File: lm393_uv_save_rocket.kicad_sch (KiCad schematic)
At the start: 13 parts, among them J1 BAT 9V, J2 IGNITER, Q1 TIP122, U1 LM7805, U2 LM393

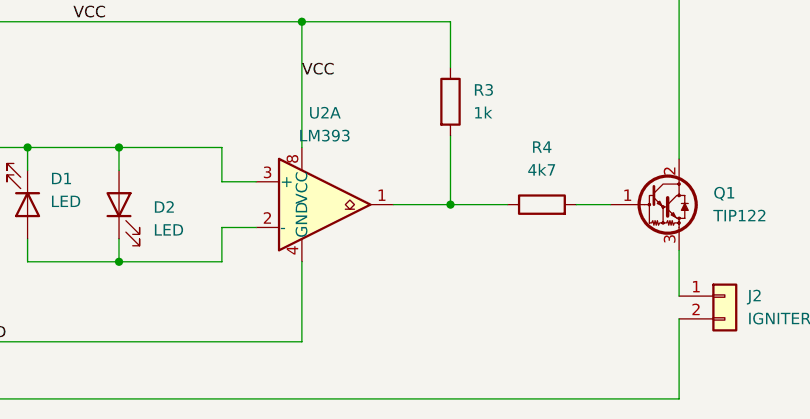
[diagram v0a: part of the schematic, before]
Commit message: Novo led que informa posição correta dos led UV, e funcionamento do circuito
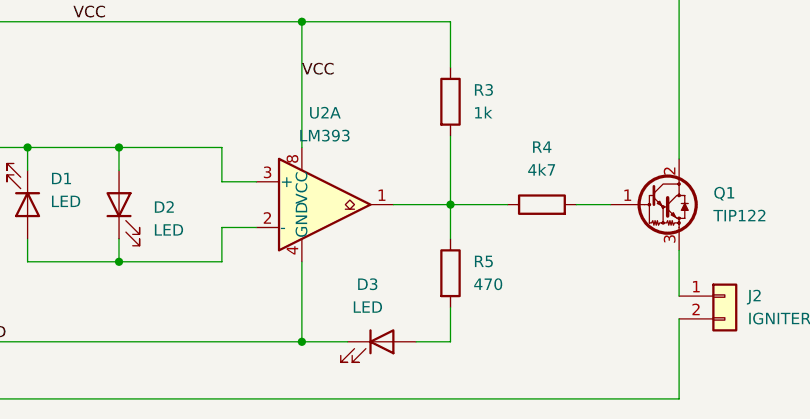
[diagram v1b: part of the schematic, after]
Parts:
- added D3: LED, LED_THT:LED_D5.0mm, symbol Device:LED
- added R5: 470, Resistor_THT:R_Axial_DIN0204_L3.6mm_D1.6mm_P5.08mm_Horizontal, symbol Device:R
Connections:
- net GND: now also D3.1 (K)
- net at R3.2, R4.1, U2.1: now also R5.1
- new net: D3.2 (A), R5.2
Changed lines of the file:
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@@
+	)
+	(junction
+		(at 129.54 63.5)
+		(diameter 0)
+		(color 0 0 0 0)
 	)
 	(junction
@@
 	(wire
 		(pts
+			(xy 146.05 48.26) (xy 146.05 52.07)
+		)
+		(stroke
+			(width 0)
+			(type default)
+		)
+	)
+	(wire
+		(pts
+			(xy 142.24 63.5) (xy 146.05 63.5)
+		)
+		(stroke
+			(width 0)
+			(type default)
+		)
+	)
+	(wire
+		(pts
 			(xy 29.21 21.59) (xy 171.45 21.59)
 		)
@@
 		(pts
 			(xy 52.07 38.1) (xy 44.45 38.1)
+		)
+		(stroke
+			(width 0)
+			(type default)
+		)
+	)
+	(wire
+		(pts
+			(xy 146.05 63.5) (xy 146.05 59.69)
+		)
+		(stroke
+			(width 0)
+			(type default)
+		)
+	)
+	(wire
+		(pts
+			(xy 129.54 63.5) (xy 134.62 63.5)
 		)
 		(stroke
@@
 	)
 	(symbol
+		(lib_id "Device:R")
+		(at 146.05 55.88 0)
+		(unit 1)
+		(exclude_from_sim no)
+		(in_bom yes)
+		(on_board yes)
+		(dnp no)
+		(fields_autoplaced yes)
+		(property "Reference" "R5"
+			(at 148.59 54.6099 0)
+			(effects
+				(font
+					(size 1.27 1.27)
+				)
+				(justify left)
+			)
+		)
+		(property "Value" "470"
+			(at 148.59 57.1499 0)
+			(effects
+				(font
+					(size 1.27 1.27)
+				)
+				(justify left)
+			)
+		)
+		(property "Footprint" "Resistor_THT:R_Axial_DIN0204_L3.6mm_D1.6mm_P5.08mm_Horizontal"
+			(at 144.272 55.88 90)
+			(effects
+				(font
+					(size 1.27 1.27)
+				)
+				(hide yes)
+			)
+		)
+		(property "Datasheet" "~"
+			(at 146.05 55.88 0)
+			(effects
+				(font
+					(size 1.27 1.27)
+				)
+				(hide yes)
+			)
+		)
+		(property "Description" "Resistor"
+			(at 146.05 55.88 0)
+			(effects
+				(font
+					(size 1.27 1.27)
+				)
+				(hide yes)
+			)
+		)
+		(pin "1"
+		)
+		(pin "2"
+		)
+		(instances
+			(project ""
+				(path "/ae093865-4f5b-4e6d-9eba-48d65543423e"
+					(reference "R5")
+					(unit 1)
+				)
+			)
+		)
+	)
+	(symbol
 		(lib_id "Comparator:LM393")
 		(at 132.08 48.26 0)
@@
 					(unit 1)
 				)
+			)
+		)
+	)
+	(symbol
+		(lib_id "Device:LED")
+		(at 138.43 63.5 0)
+		(unit 1)
+		(exclude_from_sim no)
+		(in_bom yes)
+		(on_board yes)
+		(dnp no)
+		(fields_autoplaced yes)
+		(property "Reference" "D3"
+			(at 136.8425 57.15 0)
+			(effects
+				(font
+					(size 1.27 1.27)
+				)
+			)
+		)
+		(property "Value" "LED"
+			(at 136.8425 59.69 0)
+			(effects
+				(font
+					(size 1.27 1.27)
+				)
+			)
+		)
+		(property "Footprint" "LED_THT:LED_D5.0mm"
+			(at 138.43 63.5 0)
+			(effects
+				(font
+					(size 1.27 1.27)
+				)
+				(hide yes)
+			)
+		)
+		(property "Datasheet" "~"
+			(at 138.43 63.5 0)
+			(effects
+				(font
+					(size 1.27 1.27)
+				)
+				(hide yes)
+			)
+		)
+		(property "Description" "Light emitting diode"
+			(at 138.43 63.5 0)
+			(effects
+				(font
+					(size 1.27 1.27)
+				)
+				(hide yes)
+			)
+		)
+		(property "Sim.Pins" "1=K 2=A"
+			(at 138.43 63.5 0)
+			(effects
+				(font
+					(size 1.27 1.27)
+				)
+				(hide yes)
+			)
+		)
+		(pin "1"
+		)
+		(pin "2"
+		)
+		(instances
+			(project ""
+				(path "/ae093865-4f5b-4e6d-9eba-48d65543423e"
+					(reference "D3")
+					(unit 1)
+				)

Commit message: Alteração do tipo do conector da bat 9v
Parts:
- J1: footprint TerminalBlock_Phoenix:TerminalBlock_Phoenix_MKDS-1,5-2-5.08_1x02_P5.08mm_Horizontal -> Connector_BarrelJack:BarrelJack_GCT_DCJ200-10-A_Horizontal
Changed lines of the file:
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@@
 			)
 		)
-		(property "Footprint" "TerminalBlock_Phoenix:TerminalBlock_Phoenix_MKDS-1,5-2-5.08_1x02_P5.08mm_Horizontal"
+		(property "Footprint" "Connector_BarrelJack:BarrelJack_GCT_DCJ200-10-A_Horizontal"
 			(at 24.13 45.72 0)
 			(effects

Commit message: jumper de segurança
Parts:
- added J3: IGNITER, TerminalBlock_Phoenix:TerminalBlock_Phoenix_MKDS-1,5-2-5.08_1x02_P5.08mm_Horizontal, symbol Connector_Generic:Conn_01x02
- added JP1: Jumper_2_Bridged, TestPoint:TestPoint_Bridge_Pitch5.08mm_Drill0.7mm, symbol Jumper:Jumper_2_Bridged
- J2: value IGNITER -> JUMP; footprint TerminalBlock_Phoenix:TerminalBlock_Phoenix_MKDS-1,5-2-5.08_1x02_P5.08mm_Horizontal -> Button_Switch_THT:SW_DIP_SPSTx01_Slide_6.7x4.1mm_W7.62mm_P2.54mm_LowProfile
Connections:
- net GND: now also J3.2 (Pin_2), JP1.1 (A); no longer J2.2 (Pin_2), R2.1
- new net: J2.2 (Pin_2), J3.1 (Pin_1)
- new net: JP1.2 (B), R2.1
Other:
- moved on the sheet: R2
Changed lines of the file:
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@@
 	(paper "A4")
 	(junction
-		(at 92.71 41.91)
+		(at 95.25 41.91)
 		(diameter 0)
 		(color 0 0 0 0)
@@
 	(wire
 		(pts
-			(xy 92.71 41.91) (xy 92.71 58.42)
+			(xy 95.25 41.91) (xy 95.25 58.42)
 		)
 		(stroke
@@
 	(wire
 		(pts
+			(xy 171.45 64.77) (xy 171.45 69.85)
+		)
+		(stroke
+			(width 0)
+			(type default)
+		)
+	)
+	(wire
+		(pts
 			(xy 146.05 48.26) (xy 146.05 52.07)
 		)
@@
 	(wire
 		(pts
+			(xy 29.21 69.85) (xy 157.48 69.85)
+		)
+		(stroke
+			(width 0)
+			(type default)
+		)
+	)
+	(wire
+		(pts
 			(xy 29.21 38.1) (xy 44.45 38.1)
 		)
@@
 	(wire
 		(pts
+			(xy 29.21 69.85) (xy 29.21 58.42)
+		)
+		(stroke
+			(width 0)
+			(type default)
+		)
+	)
+	(wire
+		(pts
 			(xy 129.54 63.5) (xy 134.62 63.5)
 		)
@@
 	(wire
 		(pts
-			(xy 29.21 69.85) (xy 171.45 69.85)
-		)
-		(stroke
-			(width 0)
-			(type default)
-		)
-	)
-	(wire
-		(pts
 			(xy 99.06 52.07) (xy 99.06 54.61)
 		)
@@
 	(wire
 		(pts
-			(xy 29.21 58.42) (xy 29.21 69.85)
-		)
-		(stroke
-			(width 0)
-			(type default)
-		)
-	)
-	(wire
-		(pts
 			(xy 129.54 63.5) (xy 129.54 54.61)
 		)
@@
 	(wire
 		(pts
-			(xy 171.45 53.34) (xy 171.45 58.42)
-		)
-		(stroke
-			(width 0)
-			(type default)
-		)
-	)
-	(wire
-		(pts
 			(xy 73.66 38.1) (xy 81.28 38.1)
 		)
@@
 	(wire
 		(pts
-			(xy 73.66 58.42) (xy 81.28 58.42)
+			(xy 171.45 69.85) (xy 160.02 69.85)
+		)
+		(stroke
+			(width 0)
+			(type default)
+		)
+	)
+	(wire
+		(pts
+			(xy 73.66 58.42) (xy 76.2 58.42)
 		)
 		(stroke
@@
 	(wire
 		(pts
+			(xy 86.36 58.42) (xy 87.63 58.42)
+		)
+		(stroke
+			(width 0)
+			(type default)
+		)
+	)
+	(wire
+		(pts
 			(xy 171.45 21.59) (xy 171.45 43.18)
 		)
@@
 	(wire
 		(pts
-			(xy 99.06 41.91) (xy 92.71 41.91)
+			(xy 99.06 41.91) (xy 95.25 41.91)
 		)
 		(stroke
@@
 	(wire
 		(pts
-			(xy 92.71 58.42) (xy 88.9 58.42)
-		)
-		(stroke
-			(width 0)
-			(type default)
-		)
-	)
-	(wire
-		(pts
 			(xy 29.21 58.42) (xy 44.45 58.42)
 		)
@@
 	(wire
 		(pts
+			(xy 95.25 41.91) (xy 92.71 41.91)
+		)
+		(stroke
+			(width 0)
+			(type default)
+		)
+	)
+	(wire
+		(pts
 			(xy 120.65 50.8) (xy 124.46 50.8)
 		)
@@
 	(wire
 		(pts
-			(xy 171.45 69.85) (xy 171.45 60.96)
+			(xy 171.45 53.34) (xy 171.45 62.23)
 		)
 		(stroke
@@
 	)
 	(label "GND"
-		(at 71.12 69.85 0)
+		(at 50.8 69.85 0)
 		(effects
 			(font
@@
 	)
 	(symbol
+		(lib_id "Connector_Generic:Conn_01x02")
+		(at 176.53 62.23 0)
+		(unit 1)
+		(exclude_from_sim no)
+		(in_bom yes)
+		(on_board yes)
+		(dnp no)
+		(fields_autoplaced yes)
+		(property "Reference" "J2"
+			(at 179.07 62.2299 0)
+			(effects
+				(font
+					(size 1.27 1.27)
+				)
+				(justify left)
+			)
+		)
+		(property "Value" "JUMP"
+			(at 179.07 64.7699 0)
+			(effects
+				(font
+					(size 1.27 1.27)
+				)
+				(justify left)
+			)
+		)
+		(property "Footprint" "Button_Switch_THT:SW_DIP_SPSTx01_Slide_6.7x4.1mm_W7.62mm_P2.54mm_LowProfile"
+			(at 176.53 62.23 0)
+			(effects
+				(font
+					(size 1.27 1.27)
+				)
+				(hide yes)
+			)
+		)
+		(property "Datasheet" "~"
+			(at 176.53 62.23 0)
+			(effects
+				(font
+					(size 1.27 1.27)
+				)
+				(hide yes)
+			)
+		)
+		(property "Description" "Generic connector, single row, 01x02, script generated (kicad-library-utils/schlib/autogen/connector/)"
+			(at 176.53 62.23 0)
+			(effects
+				(font
+					(size 1.27 1.27)
+				)
+				(hide yes)
+			)
+		)
+		(pin "2"
+		)
+		(pin "1"
+		)
+		(instances
+			(project "lm393_uv_save_rocket"
+				(path "/ae093865-4f5b-4e6d-9eba-48d65543423e"
+					(reference "J2")
+					(unit 1)
+				)
+			)
+		)
+	)
+	(symbol
 		(lib_id "Device:LED")
 		(at 99.06 48.26 270)
@@
 	(symbol
 		(lib_id "Device:R")
-		(at 85.09 58.42 90)
+		(at 91.44 58.42 90)
 		(unit 1)
 		(exclude_from_sim no)
@@
 		(fields_autoplaced yes)
 		(property "Reference" "R2"
-			(at 85.09 52.07 90)
+			(at 91.44 52.07 90)
 			(effects
 				(font
@@
 		)
 		(property "Value" "100k"
-			(at 85.09 54.61 90)
+			(at 91.44 54.61 90)
 			(effects
 				(font
@@
 		)
 		(property "Footprint" "Resistor_THT:R_Axial_DIN0204_L3.6mm_D1.6mm_P5.08mm_Horizontal"
-			(at 85.09 60.198 90)
+			(at 91.44 60.198 90)
 			(effects
 				(font
@@
 		)
 		(property "Datasheet" "~"
-			(at 85.09 58.42 0)
+			(at 91.44 58.42 0)
 			(effects
 				(font
@@
 		)
 		(property "Description" "Resistor"
-			(at 85.09 58.42 0)
+			(at 91.44 58.42 0)
 			(effects
 				(font
@@
 	)
 	(symbol
-		(lib_id "Connector_Generic:Conn_01x02")
-		(at 176.53 58.42 0)
+		(lib_id "Jumper:Jumper_2_Bridged")
+		(at 81.28 58.42 0)
 		(unit 1)
 		(exclude_from_sim no)
@@
 		(dnp no)
 		(fields_autoplaced yes)
-		(property "Reference" "J2"
-			(at 179.07 58.4199 0)
+		(property "Reference" "JP1"
+			(at 81.28 53.34 0)
+			(effects
+				(font
+					(size 1.27 1.27)
+				)
+			)
+		)
+		(property "Value" "Jumper_2_Bridged"
+			(at 81.28 55.88 0)
+			(effects
+				(font
+					(size 1.27 1.27)
+				)
+			)
+		)
+		(property "Footprint" "TestPoint:TestPoint_Bridge_Pitch5.08mm_Drill0.7mm"
+			(at 81.28 58.42 0)
+			(effects
+				(font
+					(size 1.27 1.27)
+				)
+				(hide yes)
+			)
+		)
+		(property "Datasheet" "~"
+			(at 81.28 58.42 0)
+			(effects
+				(font
+					(size 1.27 1.27)
+				)
+				(hide yes)
+			)
+		)
+		(property "Description" "Jumper, 2-pole, closed/bridged"
+			(at 81.28 58.42 0)
+			(effects
+				(font
+					(size 1.27 1.27)
+				)
+				(hide yes)
+			)
+		)
+		(pin "2"
+		)
+		(pin "1"
+		)
+		(instances
+			(project ""
+				(path "/ae093865-4f5b-4e6d-9eba-48d65543423e"
+					(reference "JP1")
+					(unit 1)
+				)
+			)
+		)
+	)
+	(symbol
+		(lib_id "Connector_Generic:Conn_01x02")
+		(at 160.02 74.93 270)
+		(unit 1)
+		(exclude_from_sim no)
+		(in_bom yes)
+		(on_board yes)
+		(dnp no)
+		(fields_autoplaced yes)
+		(property "Reference" "J3"
+			(at 162.56 73.6599 90)
 			(effects
 				(font
@@
 		)
 		(property "Value" "IGNITER"
-			(at 179.07 60.9599 0)
+			(at 162.56 76.1999 90)
 			(effects
 				(font
@@
 		)
 		(property "Footprint" "TerminalBlock_Phoenix:TerminalBlock_Phoenix_MKDS-1,5-2-5.08_1x02_P5.08mm_Horizontal"
-			(at 176.53 58.42 0)
+			(at 160.02 74.93 0)
 			(effects
 				(font
@@
 		)
 		(property "Datasheet" "~"
-			(at 176.53 58.42 0)
+			(at 160.02 74.93 0)
 			(effects
 				(font
@@
 		)
 		(property "Description" "Generic connector, single row, 01x02, script generated (kicad-library-utils/schlib/autogen/connector/)"
-			(at 176.53 58.42 0)
+			(at 160.02 74.93 0)
 			(effects
 				(font
@@
 		)
 		(instances
-			(project "Save_Rocket_LM393"
+			(project "lm393_uv_save_rocket"
 				(path "/ae093865-4f5b-4e6d-9eba-48d65543423e"
-					(reference "J2")
+					(reference "J3")
 					(unit 1)
 				)
